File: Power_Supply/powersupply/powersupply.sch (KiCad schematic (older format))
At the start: 68 parts, among them J1 Conn_01x03, J2 USB_B_Micro, J3 1x2, Q1 Q_PMOS_GDS, SW1 KMR2, U1 AZ1117E-3.3, U10 INA199, U2 ATSAMD10D13A-SS, U3 B0505S-2WR2, U4 TFT_OLED, U5 joystick-K1-1506DN-01, U6 MC33063AP1, U7 LM358P, U8 1x2

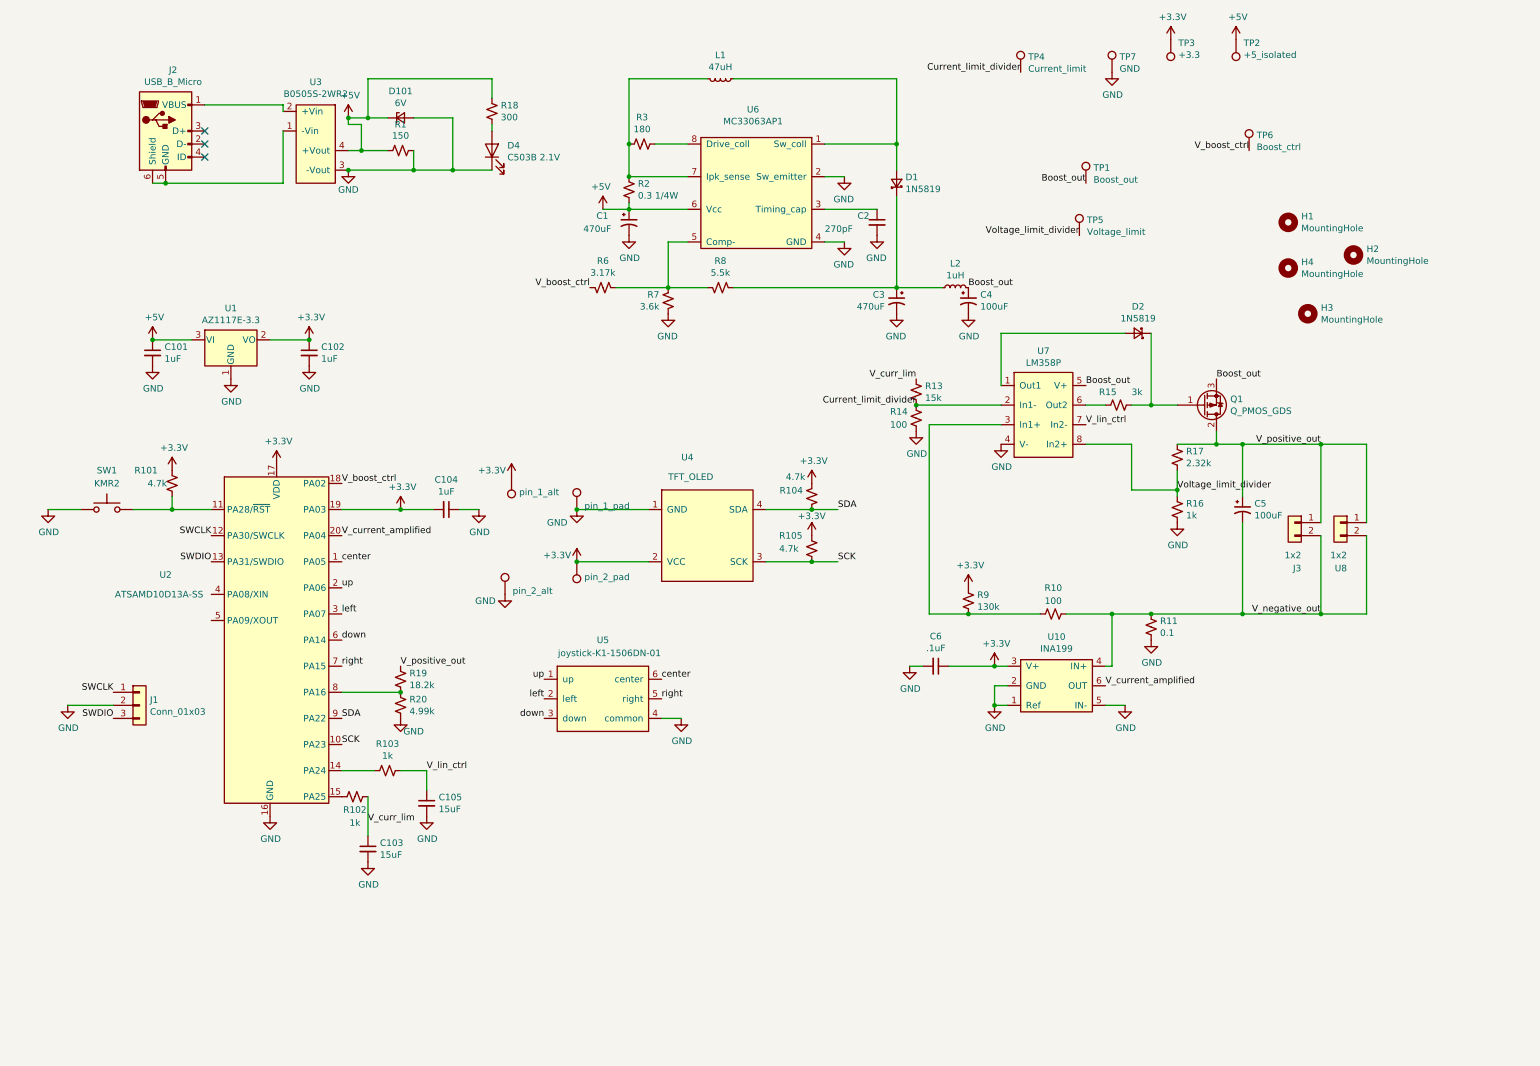
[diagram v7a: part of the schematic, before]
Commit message: schematic CHANGES
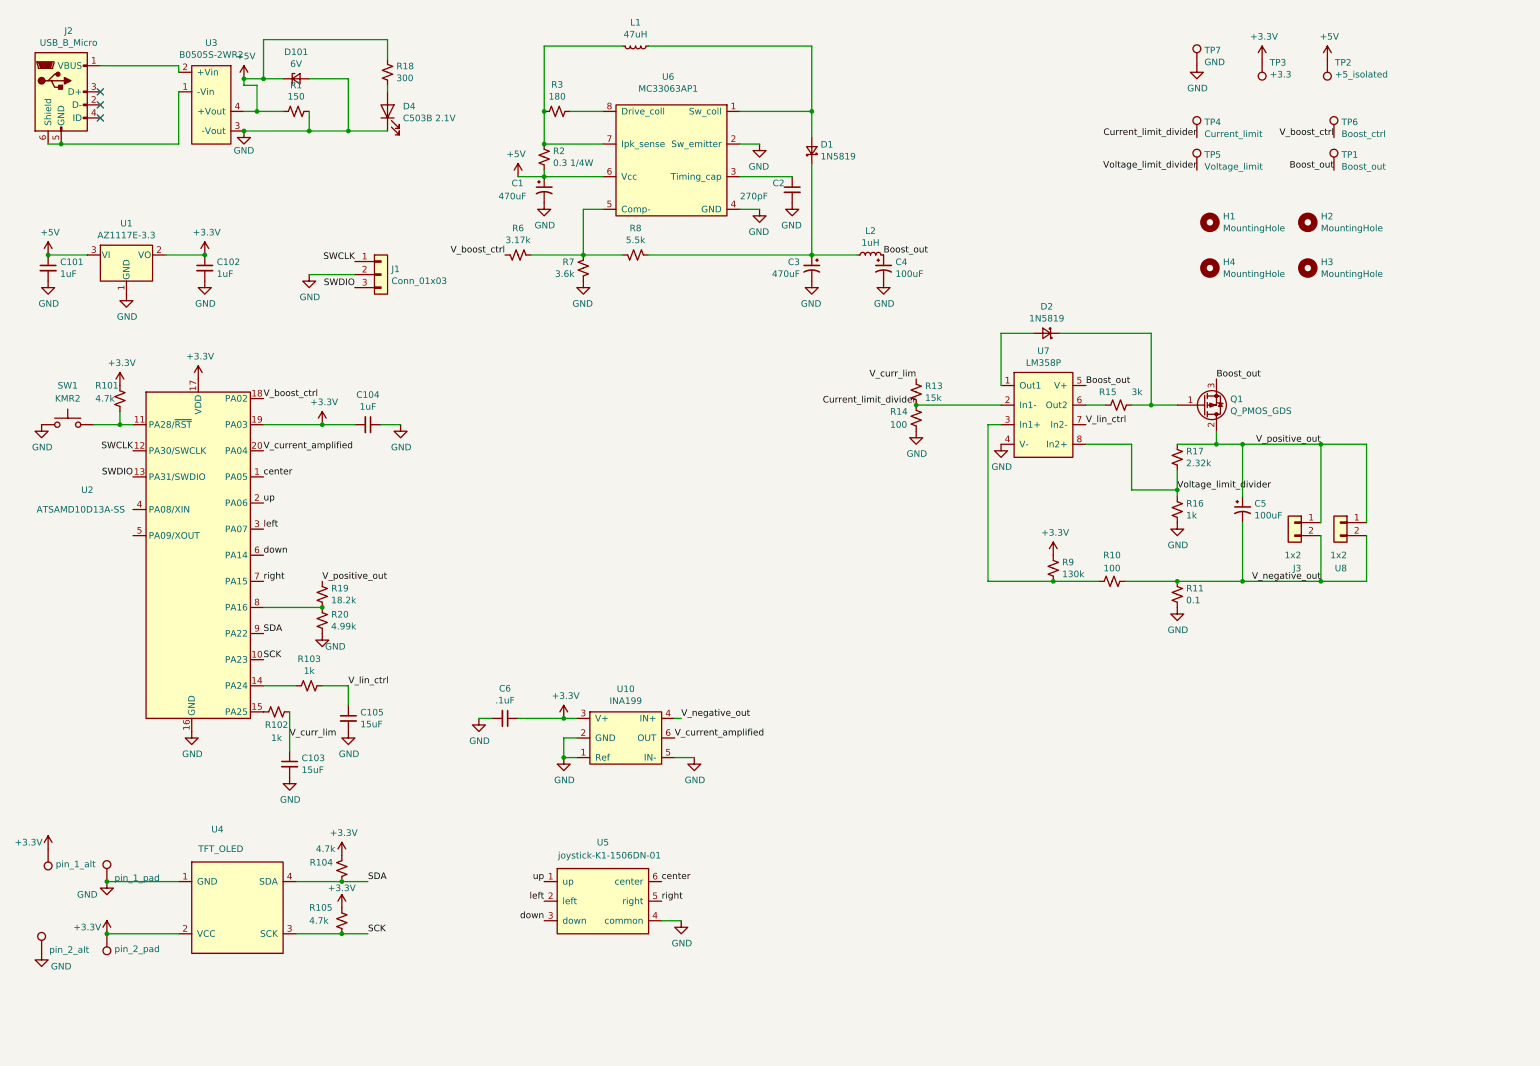
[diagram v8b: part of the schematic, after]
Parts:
- U10: footprint (none) -> Package_TO_SOT_SMD:SOT-363_SC-70-6
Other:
- moved on the sheet: C1, C101, C102, C103, C104, C105, C2, C3, C4, C6, D1, D101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
